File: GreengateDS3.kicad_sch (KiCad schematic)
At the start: 70 parts, among them IC1 74LS245, IC14 ZN448E, IC15 ZN428E, IC16 ZN428E, IC17 ZN428E, IC18 ZN428E, IC2 74LS245, IC3 MC6844, IC9 W65C22S6TPG, J1 Apple II Bus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

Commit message: adc clock, some value corrections
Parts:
- C14, C17, C23, C4, C8, C9: value 1uF -> 4.7uF
- C16: value ?? -> 0.047uF?
- C2: value 0.01uF -> ???
- J2: value Conn_01x02 -> AUD_IN
- R1: value R_Small_US -> 47 ohm 1 watt
- R2: value 12K -> 82K
- R5: value 22K -> 2.2K
- R6: value ?? -> 680?
- RN1, RN2: value ? -> 2.2K?
- RV1: value R_Potentiometer -> LEVEL
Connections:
- net ADC_CLK: now also U9.37 (OUT5)
- net VREF_1V25: now reaches C23.1, R13.2, R8.2, U10.3 (+)
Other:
- note added: "Assuming 10K input impedance for next stage"
- note added: "Confirm resistance"
- note added: "Input range is 0 to 2.5V"
- note added: "Max +/-1.25V"
- note added: "Max sample rate 30K Nyquist 15KHz"
- note added: "Maybe 470pF?"
- note added: "Probably 5K-20K"
- note added: "Unknown delay cap Probably ~100pF"
- note added: "Vout=0 to 2.5V 0.78Vp-p"
- note added: "fc=15KHz"
- moved on the sheet: C14, C19, R1, R13, R18, R8

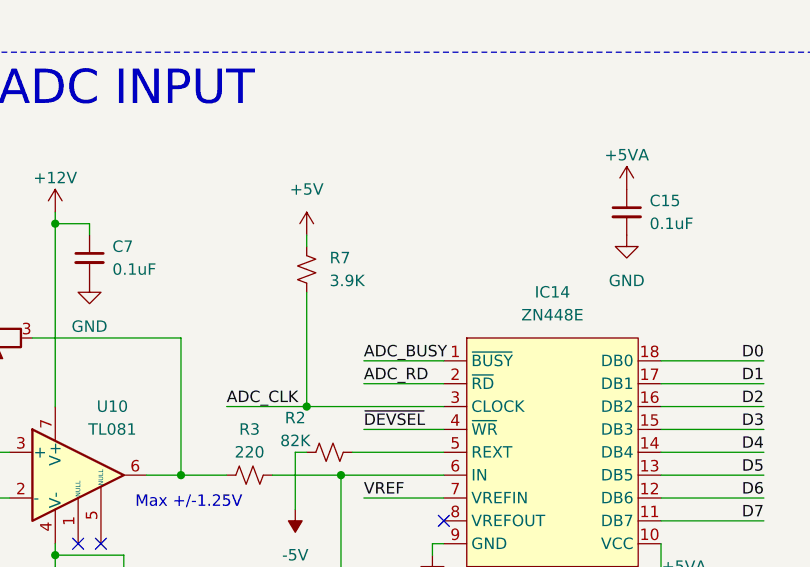
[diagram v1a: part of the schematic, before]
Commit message: minor part value changes
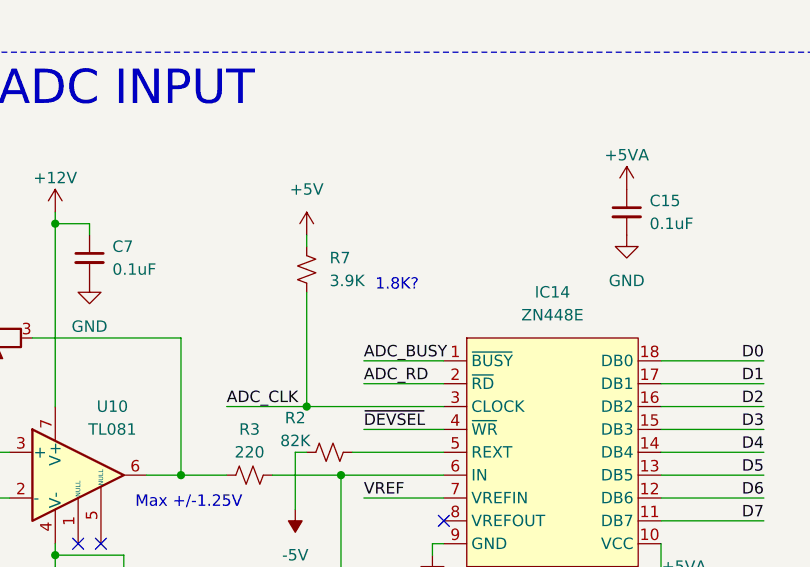
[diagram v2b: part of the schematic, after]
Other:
- note added: "1.8K?"
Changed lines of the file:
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@@
     (effects (font (size 2.54 2.54)) (justify left bottom))
+  )
+  (text "1.8K?" (at 438.15 59.69 0)
+    (effects (font (size 1.27 1.27)) (justify left bottom))
   )
   (text "Confirm resistance" (at 163.83 353.06 0)

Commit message: fabout
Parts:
- R1: Mouser (none) -> 279-CFR100J47R
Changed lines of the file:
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@@
+      (effects (font (size 1.27 1.27)) hide)
+    )
+    (property "Mouser" "279-CFR100J47R" (at 257.81 69.85 0)
       (effects (font (size 1.27 1.27)) hide)
     )

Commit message: Minor schematic tweaks
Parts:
- C10, C12, C13: value ?? -> 470pF
- C11: value ?? -> 480pF
- C16: value 0.047uF? -> 0.047uF
- C2: value ??? -> 220pF
- IC9: value W65C22S6TPG -> 6522
- R6: value 680? -> 680
- RN1, RN2: value 2.2K? -> 10K
- RV1: value LEVEL -> 10K
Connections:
- no-connect marks 6 -> 8
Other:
- note added: "1"
- note added: "10"
- note added: "11"
- note added: "12"
- note added: "13"
- note added: "14"
- note added: "15"
- note added: "16"
- note added: "2"
- note added: "3"
- note added: "4"
- note added: "5"
- note added: "6"
- note added: "7"
- note added: "8"
- note added: "9"
- note added: "Delay cap should be between 220pF and 680pF"
- note added: "Goodgreat DS3"
- note added: "NMOS ONLY WDC65C22 WILL NOT WORK!"
- note added: "OCTAVE ORDER: PA0-PA7: 0, 1, 2, 3, 4, 5, 6, 7 NOTE ORDER: PB0-PB7: 4, 1, 3, 0, 2, 6, 7, 5 KEYBOARD DIODES IN SERIES WITH KEYS ANODES: NOTE LINES CATHODES: OCTAVE LINES"
- note added: "PA0-PA7: OCTAVE LINES (ACTIVE LOW) PB0-PB7: INPUTS (NOTES)"
- note removed: "1.8K?"
- note removed: "Confirm resistance"
- note removed: "GREENGATE DS:3"
- note removed: "Greengate DS:3"
- note removed: "Unknown delay cap Probably ~100pF"
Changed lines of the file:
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@@
   (no_connect (at 445.77 85.09))
   (no_connect (at 405.13 87.63))
+  (no_connect (at 217.17 69.85))
   (no_connect (at 407.67 87.63))
+  (no_connect (at 204.47 92.71))
   (no_connect (at 151.13 323.85))
   (no_connect (at 151.13 318.77))
@@
     (effects (font (size 1.27 1.27)) (justify left bottom))
   )
-  (text "Unknown delay cap\nProbably ~100pF" (at 339.09 187.96 0)
+  (text "Delay cap should be between 220pF and 680pF" (at 328.93 189.23 0)
+    (effects (font (size 1.27 1.27)) (justify left bottom))
+  )
+  (text "13" (at 201.93 87.63 0)
     (effects (font (size 1.27 1.27)) (justify left bottom))
   )
@@
     (effects (font (size 3.81 3.81)) (justify left bottom))
   )
-  (text "GREENGATE DS:3" (at 250.19 26.67 0)
+  (text "Goodgreat DS3" (at 250.19 26.67 0)
     (effects (font (size 6.35 6.35)) (justify left bottom))
   )
+  (text "7" (at 201.93 80.01 0)
+    (effects (font (size 1.27 1.27)) (justify left bottom))
+  )
   (text "Maybe 470pF?" (at 311.15 269.24 0)
     (effects (font (size 1.27 1.27)) (justify left bottom))
   )
+  (text "6" (at 218.44 77.47 0)
+    (effects (font (size 1.27 1.27)) (justify left bottom))
+  )
+  (text "PA0-PA7: OCTAVE LINES (ACTIVE LOW)\nPB0-PB7: INPUTS (NOTES)"
+    (at 196.85 58.42 0)
+    (effects (font (size 1.27 1.27)) (justify left bottom))
+  )
+  (text "15" (at 201.93 90.17 0)
+    (effects (font (size 1.27 1.27)) (justify left bottom))
+  )
   (text "This work is licensed under the Creative Commons\nAttribute-ShareAlike 4.0 International License.\nTo view a copy of this license, visit\nhttp://creativecommons.org/license/by-sa/4.0/\nor send a letter to Creative Commons, PO Box 1866,\nMountain View, CA 94042, USA."
     (at 365.76 401.32 0)
@@
     (effects (font (size 2.54 2.54)) (justify left bottom))
   )
-  (text "1.8K?" (at 438.15 59.69 0)
+  (text "9" (at 201.93 82.55 0)
     (effects (font (size 1.27 1.27)) (justify left bottom))
   )
-  (text "Confirm resistance" (at 163.83 353.06 0)
-    (effects (font (size 1.27 1.27)) (justify right bottom))
+  (text "2" (at 218.44 72.39 0)
+    (effects (font (size 1.27 1.27)) (justify left bottom))
+  )
+  (text "8" (at 218.44 80.01 0)
+    (effects (font (size 1.27 1.27)) (justify left bottom))
+  )
+  (text "11" (at 201.93 85.09 0)
+    (effects (font (size 1.27 1.27)) (justify left bottom))
   )
   (text "DMA ARB/GNT STATE MACHINE" (at 360.68 148.59 0)
@@
     (effects (font (size 1.27 1.27)) (justify left bottom))
   )
+  (text "14" (at 218.44 87.63 0)
+    (effects (font (size 1.27 1.27)) (justify left bottom))
+  )
+  (text "OCTAVE ORDER:\nPA0-PA7: 0, 1, 2, 3, 4, 5, 6, 7\n\nNOTE ORDER:\nPB0-PB7: 4, 1, 3, 0, 2, 6, 7, 5\n\nKEYBOARD DIODES IN SERIES WITH KEYS\nANODES: NOTE LINES\nCATHODES: OCTAVE LINES"
+    (at 199.39 119.38 0)
+    (effects (font (size 1.27 1.27)) (justify left bottom))
+  )
+  (text "3" (at 201.93 74.93 0)
+    (effects (font (size 1.27 1.27)) (justify left bottom))
+  )
   (text "ADDRESS DECODER" (at 85.09 203.2 0)
     (effects (font (size 3.81 3.81)) (justify left bottom))
@@
     (effects (font (size 3.81 3.81)) (justify left bottom))
   )
+  (text "10" (at 218.44 82.55 0)
+    (effects (font (size 1.27 1.27)) (justify left bottom))
+  )
   (text "FOUR DAC OUTPUTS" (at 252.73 234.95 0)
     (effects (font (size 3.81 3.81)) (justify left bottom))
   )
+  (text "12" (at 218.44 85.09 0)
+    (effects (font (size 1.27 1.27)) (justify left bottom))
+  )
+  (text "16" (at 218.44 90.17 0)
+    (effects (font (size 1.27 1.27)) (justify left bottom))
+  )
   (text "BYPASS CAPACITORS" (at 402.59 240.03 0)
     (effects (font (size 3.81 3.81)) (justify left bottom))
@@
     (effects (font (size 3.81 3.81)) (justify left bottom))
   )
+  (text "1" (at 201.93 72.39 0)
+    (effects (font (size 1.27 1.27)) (justify left bottom))
+  )
   (text "ADC INPUT" (at 396.24 39.37 0)
     (effects (font (size 3.81 3.81)) (justify left bottom))
@@
     (effects (font (size 1.27 1.27)) (justify left bottom))
   )
-  (text "Greengate DS:3" (at 477.52 384.81 0)
+  (text "Goodgreat DS3" (at 477.52 384.81 0)
     (effects (font (size 5.08 5.08)) (justify left bottom))
   )
@@
     (effects (font (size 1.27 1.27)) (justify left bottom))
   )
+  (text "NMOS ONLY\nWDC65C22 WILL NOT WORK!" (at 173.99 50.8 0)
+    (effects (font (size 1.27 1.27)) (justify left bottom))
+  )
+  (text "4" (at 218.44 74.93 0)
+    (effects (font (size 1.27 1.27)) (justify left bottom))
+  )
+  (text "5" (at 201.93 77.47 0)
+    (effects (font (size 1.27 1.27)) (justify left bottom))
+  )
   (text "Max sample rate 30K\nNyquist 15KHz" (at 447.04 109.22 0)
     (effects (font (size 1.27 1.27)) (justify left bottom))
@@
       (effects (font (size 1.524 1.524)) (justify left))
     )
-    (property "Value" "W65C22S6TPG" (at 164.7541 50.8 0)
+    (property "Value" "6522" (at 164.7541 50.8 0)
       (effects (font (size 1.524 1.524)) (justify left))
     )
@@
   )
   (symbol (lib_id "Device:C_Small") (at 308.61 261.62 0) (mirror y) (unit 1)
-    (in_bom yes) (on_board yes) (dnp no) (fields_autoplaced)
-    (property "Reference" "C13" (at 306.07 260.3563 0)
-      (effects (font (size 1.27 1.27)) (justify left))
+    (in_bom yes) (on_board yes) (dnp no)
+    (property "Reference" "C13" (at 302.26 260.35 0)
+      (effects (font (size 1.27 1.27)) (justify right))
     )
-    (property "Value" "??" (at 306.07 262.8963 0)
-      (effects (font (size 1.27 1.27)) (justify left))
+    (property "Value" "470pF" (at 300.99 262.89 0)
+      (effects (font (size 1.27 1.27)) (justify right))
     )
     (property "Footprint" "Passive:CAPAC200" (at 308.61 261.62 0)
@@
       (effects (font (size 1.27 1.27)) (justify left))
     )
-    (property "Value" "???" (at 349.25 175.2663 0)
+    (property "Value" "220pF" (at 349.25 175.2663 0)
       (effects (font (size 1.27 1.27)) (justify left))
     )
@@
       (effects (font (size 1.27 1.27)) (justify left))
     )
-    (property "Value" "0.047uF?" (at 436.88 96.52 0)
+    (property "Value" "0.047uF" (at 436.88 96.52 0)
       (effects (font (size 1.27 1.27)) (justify left))
     )
@@
       (effects (font (size 1.27 1.27)) (justify right))
     )
-    (property "Value" "680?" (at 146.05 345.44 0)
+    (property "Value" "680" (at 146.05 345.44 0)
       (effects (font (size 1.27 1.27)) (justify right))
     )
@@
       (effects (font (size 1.27 1.27)) (justify right))
     )
-    (property "Value" "LEVEL" (at 386.08 60.96 90)
+    (property "Value" "10K" (at 386.08 60.96 90)
       (effects (font (size 1.27 1.27)) (justify right))
     )
@@
   )
   (symbol (lib_id "Device:C_Small") (at 309.88 365.76 0) (mirror y) (unit 1)
-    (in_bom yes) (on_board yes) (dnp no) (fields_autoplaced)
-    (property "Reference" "C10" (at 307.34 364.4963 0)
-      (effects (font (size 1.27 1.27)) (justify left))
+    (in_bom yes) (on_board yes) (dnp no)
+    (property "Reference" "C10" (at 300.99 364.49 0)
+      (effects (font (size 1.27 1.27)) (justify right))
     )
-    (property "Value" "??" (at 307.34 367.0363 0)
-      (effects (font (size 1.27 1.27)) (justify left))
+    (property "Value" "470pF" (at 300.99 367.03 0)
+      (effects (font (size 1.27 1.27)) (justify right))
     )
     (property "Footprint" "Passive:CAPAC200" (at 309.88 365.76 0)
@@
       (effects (font (size 1.27 1.27)))
     )
-    (property "Value" "2.2K?" (at 102.616 83.82 90)
+    (property "Value" "10K" (at 102.616 83.82 90)
       (effects (font (size 1.27 1.27)))
     )
@@
   )
   (symbol (lib_id "Device:C_Small") (at 308.61 327.66 0) (mirror y) (unit 1)
-    (in_bom yes) (on_board yes) (dnp no) (fields_autoplaced)
-    (property "Reference" "C11" (at 306.07 326.3963 0)
-      (effects (font (size 1.27 1.27)) (justify left))
+    (in_bom yes) (on_board yes) (dnp no)
+    (property "Reference" "C11" (at 299.72 326.39 0)
+      (effects (font (size 1.27 1.27)) (justify right))
     )
-    (property "Value" "??" (at 306.07 328.9363 0)
-      (effects (font (size 1.27 1.27)) (justify left))
+    (property "Value" "480pF" (at 299.72 328.93 0)
+      (effects (font (size 1.27 1.27)) (justify right))
     )
     (property "Footprint" "Passive:CAPAC200" (at 308.61 327.66 0)
@@
   )
   (symbol (lib_id "Device:C_Small") (at 309.88 293.37 0) (mirror y) (unit 1)
-    (in_bom yes) (on_board yes) (dnp no) (fields_autoplaced)
-    (property "Reference" "C12" (at 307.34 292.1063 0)
-      (effects (font (size 1.27 1.27)) (justify left))
+    (in_bom yes) (on_board yes) (dnp no)
+    (property "Reference" "C12" (at 300.99 292.1 0)
+      (effects (font (size 1.27 1.27)) (justify right))
     )
-    (property "Value" "??" (at 307.34 294.6463 0)
-      (effects (font (size 1.27 1.27)) (justify left))
+    (property "Value" "470pF" (at 300.99 294.64 0)
+      (effects (font (size 1.27 1.27)) (justify right))
     )
     (property "Footprint" "Passive:CAPAC200" (at 309.88 293.37 0)
@@
       (effects (font (size 1.27 1.27)))
     )
-    (property "Value" "2.2K?" (at 102.616 52.07 90)
+    (property "Value" "10K" (at 102.616 52.07 90)
       (effects (font (size 1.27 1.27)))
     )

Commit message: Fix C11 value
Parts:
- C11: value 480pF -> 470pF
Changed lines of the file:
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@@
       (effects (font (size 1.27 1.27)) (justify right))
     )
-    (property "Value" "480pF" (at 299.72 328.93 0)
+    (property "Value" "470pF" (at 299.72 328.93 0)
       (effects (font (size 1.27 1.27)) (justify right))
     )
